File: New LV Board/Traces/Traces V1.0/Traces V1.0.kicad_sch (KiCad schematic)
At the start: 11 parts, among them J1 B15B-PH-K-S, J2 B15B-PH-K-S, J3 B15B-PH-K-S, J4 Conn_01x12, J6 Conn_01x12, J7 Conn_01x12

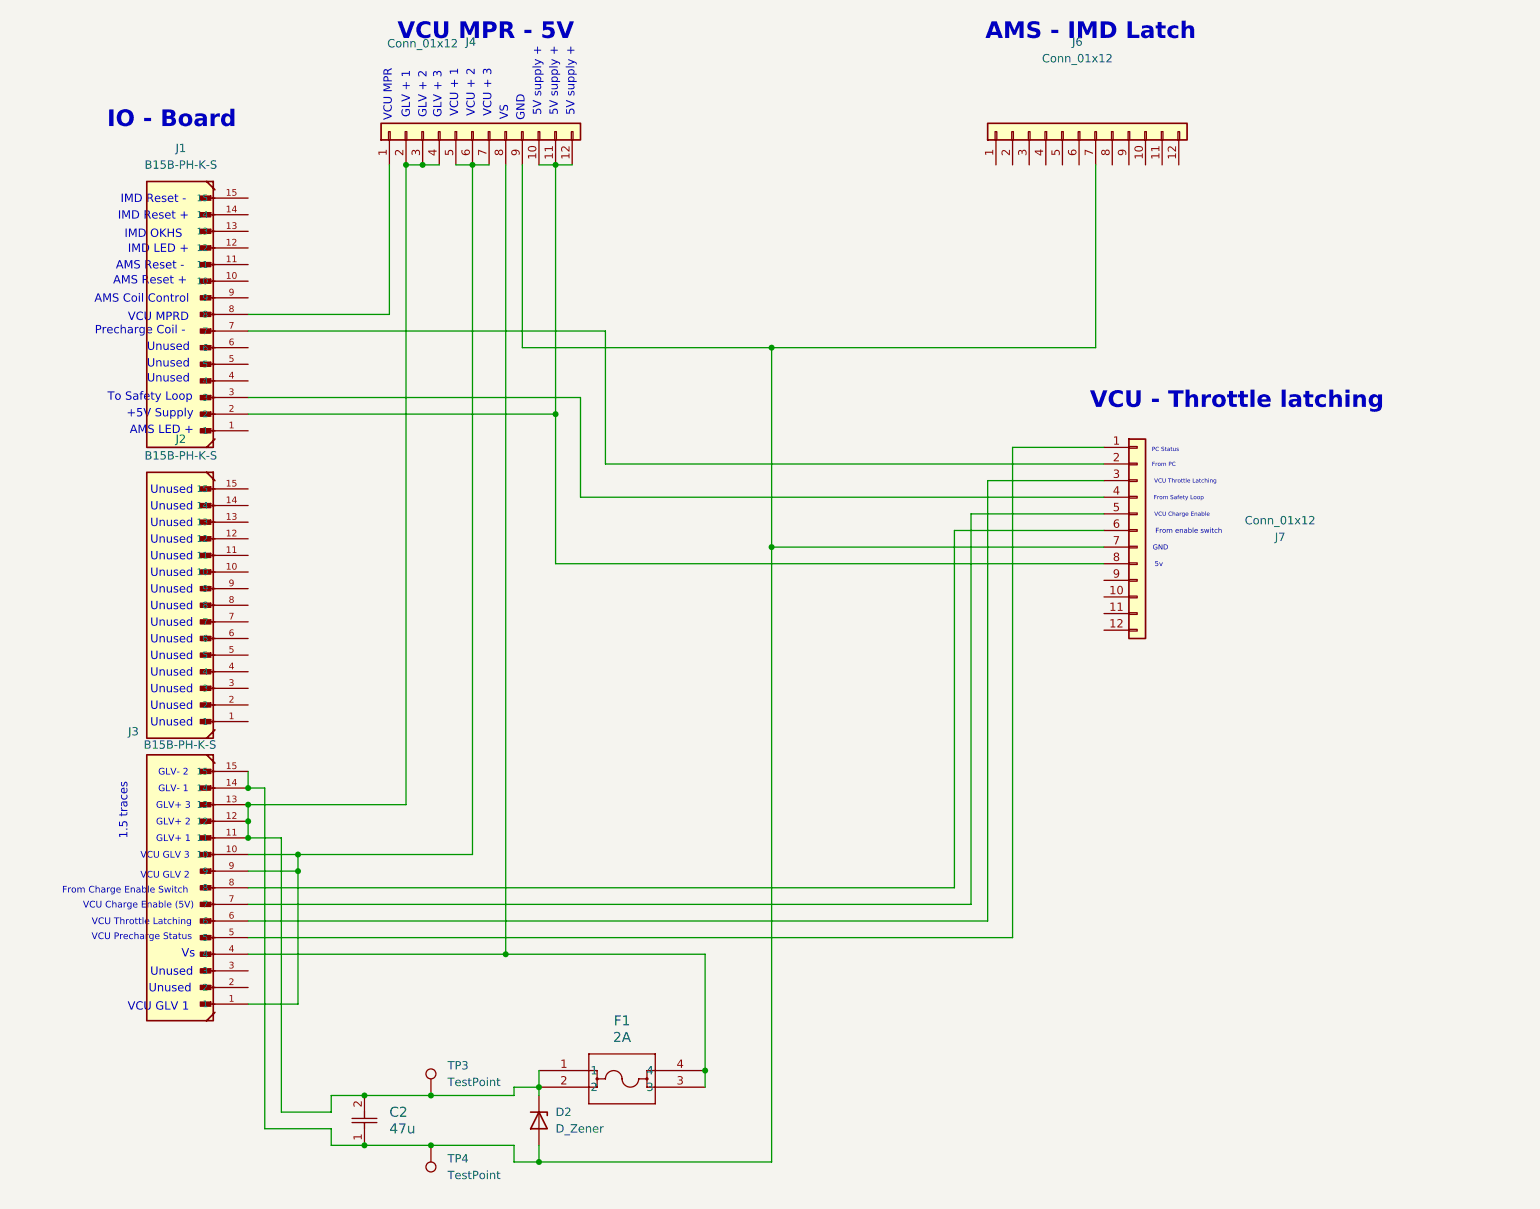
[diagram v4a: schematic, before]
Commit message: traces board changed to add VCU MPR - 5V connections
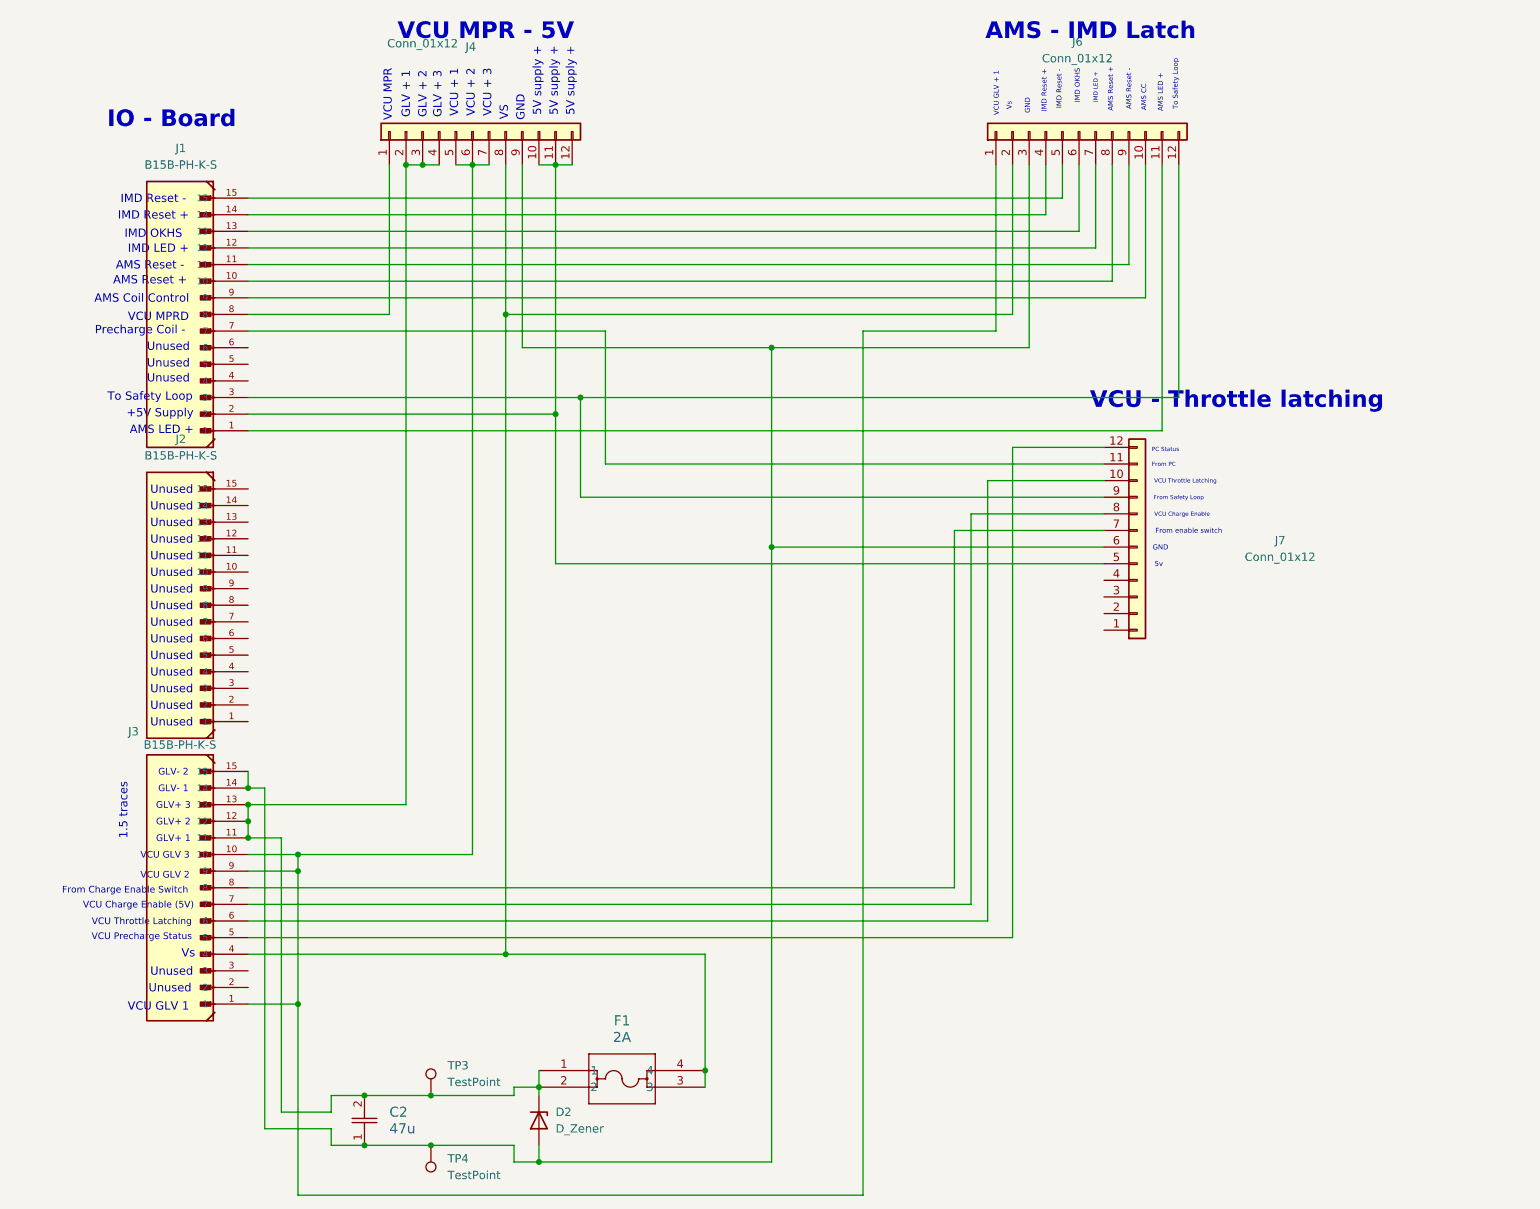
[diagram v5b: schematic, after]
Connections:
- net at J1.1: now also J6.11 (Pin_11)
- net at J1.10: now also J6.8 (Pin_8)
- net at J1.11: now also J6.9 (Pin_9)
- net at J1.12: now also J6.7 (Pin_7)
- net at J1.13: now also J6.6 (Pin_6)
- net at J1.14: now also J6.4 (Pin_4)
- net at J1.15: now also J6.5 (Pin_5)
- net at J1.2, J4.10 (Pin_10), J4.11 (Pin_11)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: now also J7.5 (Pin_5); no longer J7.8 (Pin_8)
- net at J1.3: now also J6.12 (Pin_12), J7.9 (Pin_9); no longer J7.4 (Pin_4)
- net at J1.7: now also J7.11 (Pin_11); no longer J7.2 (Pin_2)
- net at J1.9: now also J6.10 (Pin_10)
- net at F1.3, F1.4, J3.4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: now also J6.2 (Pin_2)
- net at J7.1 (Pin_1): no longer J3.5
- net at J7.10 (Pin_10): now also J3.6
- net at J7.12 (Pin_12): now also J3.5
- net at J7.3 (Pin_3): no longer J3.6
- net at J3.7: now also J7.8 (Pin_8); no longer J7.5 (Pin_5)
- net at J7.6 (Pin_6): now also C2.1, D2.2 (A), J3.14, J3.15, J4.9 (Pin_9), J6.3 (Pin_3), TP4.1; no longer J3.8
- net at J3.1, J3.10, J3.9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: now also J6.1 (Pin_1)
- new net: J3.8, J7.7 (Pin_7)
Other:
- note added: "AMS CC"
- note added: "VCU GLV + 1"

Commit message: traces probably
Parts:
- added J5: B12B-PH-K-S, Connector_JST:JST_PH_B12B-PH-K_1x12_P2.00mm_Vertical, symbol Connector_Generic:Conn_01x12
- J1, J2, J3: footprint motorsports:JST_B15B-PH-K-S -> Connector_JST:JST_PH_B15B-PH-K_1x15_P2.00mm_Vertical
- J4, J6, J7: value Conn_01x12 -> B12B-PH-K-S; footprint motorsports:JST_B12B-PH-K-S -> Connector_JST:JST_PH_B12B-PH-K_1x12_P2.00mm_Vertical
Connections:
- net at J6.11 (Pin_11): now also F1.3, F1.4, J3.12, J4.5 (Pin_5), J5.12 (Pin_12); no longer J1.1
- net at J6.8 (Pin_8): now also J1.1; no longer J1.10
- net at J1.11: now also J7.2 (Pin_2); no longer J6.9 (Pin_9)
- net at J1.12: now also J1.10; no longer J6.7 (Pin_7)
- net at J1.13: now also J6.1 (Pin_1), J7.9 (Pin_9); no longer J6.6 (Pin_6)
- net at J1.14: now also J4.1 (Pin_1), J4.2 (Pin_2), J4.3 (Pin_3), J7.5 (Pin_5), J5.10 (Pin_10); no longer J6.4 (Pin_4)
- net at J1.15: now also J6.2 (Pin_2); no longer J6.5 (Pin_5)
- net at J1.4: now also J6.6 (Pin_6)
- net at J1.5: now also J6.4 (Pin_4)
- net at J1.6: now also J6.5 (Pin_5)
- net at J1.7: now also J6.3 (Pin_3); no longer J7.11 (Pin_11)
- net at J1.8: now also J4.12 (Pin_12); no longer J4.1 (Pin_1)
- net at J6.10 (Pin_10): now also C2.1, D2.2 (A), J3.1, J3.2, J4.4 (Pin_4), J7.6 (Pin_6), TP4.1, J5.11 (Pin_11); no longer J1.9
- net at J7.10 (Pin_10): now also J3.10; no longer J3.6
- net at J3.5: now also C2.2, D2.1 (K), F1.1, F1.2, J3.3, J3.4, J4.10 (Pin_10), J4.11 (Pin_11), J4.9 (Pin_9), TP3.1; no longer J7.12 (Pin_12)
- net at J7.3 (Pin_3): now also J2.1
- net at J7.4 (Pin_4): now also J2.2
- net at J7.8 (Pin_8): now also J3.9; no longer J3.7
- net at J2.5: now also J5.9 (Pin_9)
- net at J2.6: now also J5.8 (Pin_8)
- net at J2.7: now also J5.7 (Pin_7)
- net at J2.8: now also J5.6 (Pin_6)
- new net: J1.2, J6.9 (Pin_9)
- new net: J1.3, J6.7 (Pin_7)
- new net: J1.9, J7.11 (Pin_11)
- new net: J3.11, J7.12 (Pin_12)
- new net: J3.15, J3.6, J3.7, J4.6 (Pin_6), J4.7 (Pin_7), J4.8 (Pin_8), J6.12 (Pin_12)
- now unconnected: J3.13, J3.14
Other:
- note added: "1 2 3 4 5 6 7 8 9 10 11 12"
- note added: "15 14 13 12 11 10 9 8 7 6 5 4 3 2 1"
- note added: "5V+"
- note added: "GLV +"
- note added: "Hall Effect Vref In"
- note added: "Heffect In"
- note added: "Potential Board"
- note added: "RTDS Power -"
- note added: "RTDS VCU"
- note added: "Reserved Input 1"
- note added: "Reserved Input 2"
- note added: "Reserved Input 3"
- note added: "Reserved Input 4"
- note added: "VCU Signals"
- note added: "Vout"
- note added: "Vref In"
- note removed: "VCU - Throttle latching"
- note removed: "VCU GLV + 1"
- moved on the sheet: J1, J2, J3, J4, J6

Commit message: Changed some labels
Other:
- note added: "From charge enable"
- note added: "VCU MPR - 5V (VCU labels suck)"
- note removed: "From enable switch"
- note removed: "VCU MPR - 5V"
- note removed: "VCU MPRD"
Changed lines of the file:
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@@
 		)
 	)
-	(text "VCU MPRD"
+	(text "VCU MPR"
 		(exclude_from_sim no)
 		(at 45.974 60.198 0)
@@
 		)
 	)
-	(text "From enable switch"
+	(text "From charge enable"
 		(exclude_from_sim no)
 		(at 203.454 92.964 0)
@@
 		)
 	)
-	(text "VCU MPR - 5V"
+	(text "VCU MPR - 5V (VCU labels suck)"
 		(exclude_from_sim no)
 		(at 96.012 16.51 0)

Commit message: BANG
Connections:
- net at J7.8 (Pin_8): no longer J3.9
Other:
- note added: "From Precharge"
- note added: "From charge enable switch"
- note added: "GLV+"
- note added: "GLV-"
- note added: "GND (GLV-)"
- note added: "Heffect Out"
- note added: "Temp sensor pull up"
- note added: "VCU GLV+"
- note added: "VCU MPRD"
- note added: "VCU MPRD - 5V Converter"
- note removed: "5V supply +"
- note removed: "From charge enable"
- note removed: "GLV + 1"
- note removed: "GLV + 2"
- note removed: "GLV + 3"
- note removed: "GLV+ 1"
- note removed: "GLV+ 2"
- note removed: "GLV+ 3"
- note removed: "GLV- 1"
- note removed: "GLV- 2"
- note removed: "PC Status"
- note removed: "Precharge Coil -"
- note removed: "VCU + 1"
- note removed: "VCU + 2"
- note removed: "VCU + 3"
- note removed: "VCU Charge Enable (5V)"
- note removed: "VCU GLV 1"
- note removed: "VCU GLV 2"
- note removed: "VCU GLV 3"
- note removed: "VCU MPR"
- note removed: "VCU MPR - 5V (VCU labels suck)"
- note removed: "Vout"
- moved on the sheet: F1
